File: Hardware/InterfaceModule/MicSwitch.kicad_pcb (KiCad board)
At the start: 2 copper layers, 76 x 76 mm, 21 parts, among them J10 External MIC IN, J6 D-700 MIC, J7 TS-480 MIC, J8 D-700 EXT.SP 1, J9 TS-480 EXT.SP, K1 FINDER-40.52, K2 FINDER-40.52, K3 FINDER-40.52, K4 FINDER-40.52, K5 FINDER-40.52, K6 FINDER-40.52, K7 FINDER-40.52, K8 FINDER-40.52

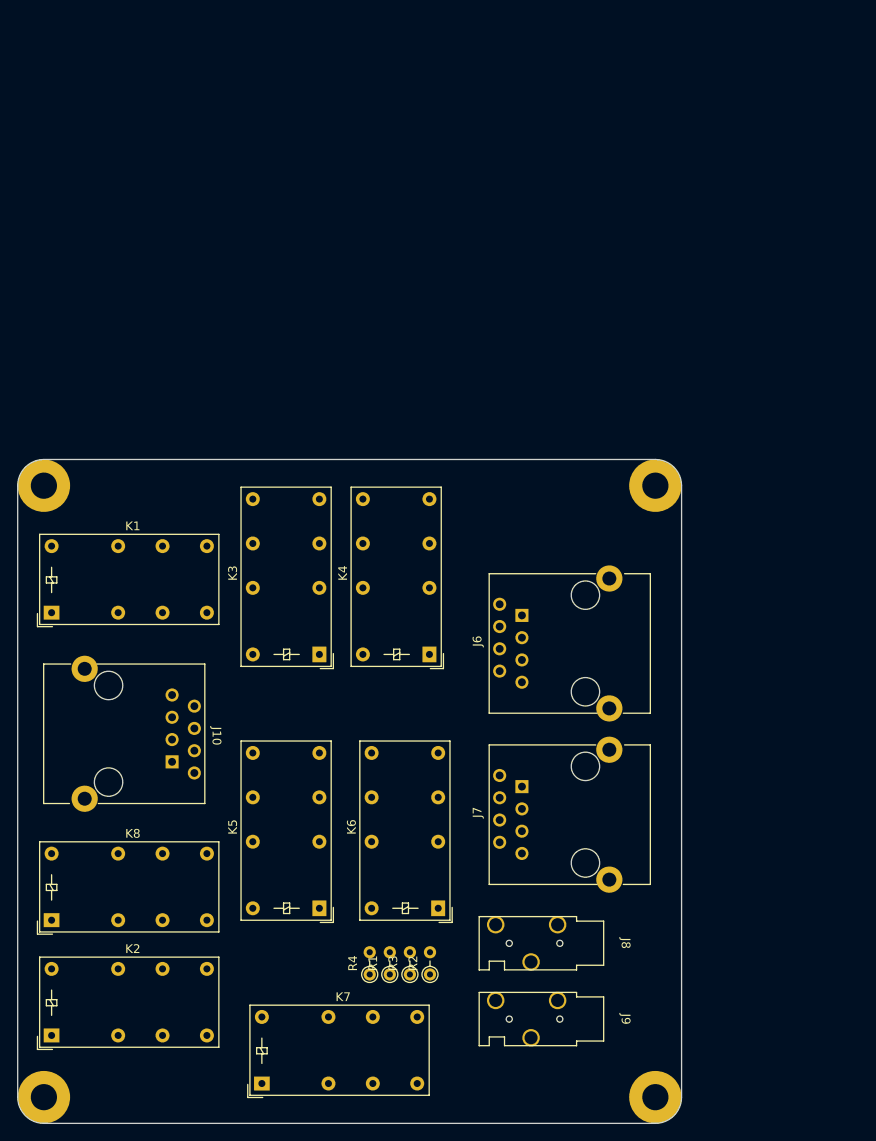
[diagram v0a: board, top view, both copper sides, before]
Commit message: Updated silkscreen dates, corrected gerber files
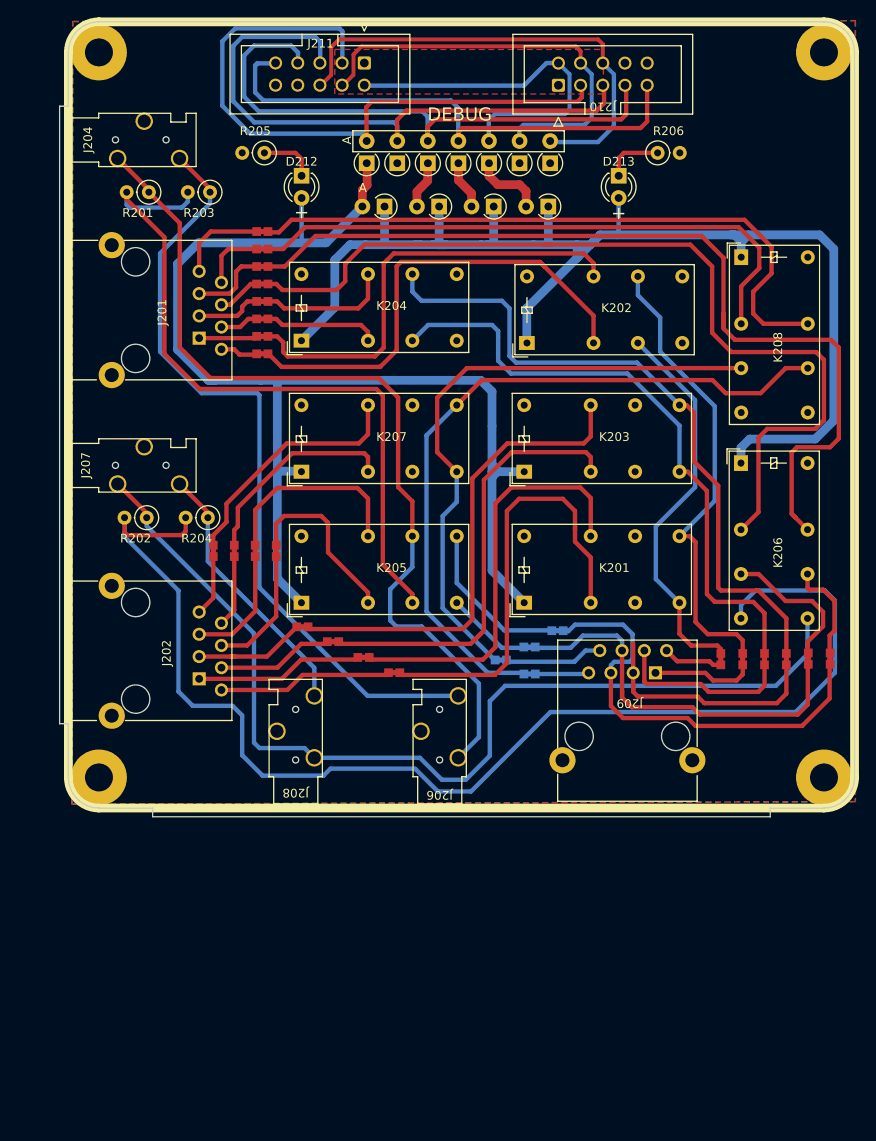
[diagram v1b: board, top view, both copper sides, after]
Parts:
- removed H1, H2, H3, H4: MountingHole_Pad, 
- removed J10: External MIC IN, libraries:Mystery_RJ45
- removed J6: D-700 MIC, libraries:Mystery_RJ45
- removed J7: TS-480 MIC, libraries:Mystery_RJ45
- removed J8: D-700 EXT.SP 1, libraries:Mystery_3.5mm
- removed J9: TS-480 EXT.SP, libraries:Mystery_3.5mm
- removed K1, K2, K3, K4, K5, K6, K7, K8: FINDER-40.52, Relay_THT:Relay_DPDT_Finder_30.22
- removed R1, R2: 3.9Ohm, Resistor_THT:R_Axial_DIN0204_L3.6mm_D1.6mm_P2.54mm_Vertical
- removed R3, R4: 470Ohm, Resistor_THT:R_Axial_DIN0204_L3.6mm_D1.6mm_P2.54mm_Vertical
- added D201: D_Small_Filled, Diode_THT:D_A-405_P2.54mm_Vertical_AnodeUp, F.Cu at (141.7, 26.7)
- added D202: D_Small_Filled, Diode_THT:D_A-405_P2.54mm_Vertical_AnodeUp, F.Cu at (145.2, 26.7)
- added D203: D_Small_Filled, Diode_THT:D_A-405_P2.54mm_Vertical_AnodeUp, F.Cu at (148.7, 26.7)
- added D204: D_Small_Filled, Diode_THT:D_A-405_P2.54mm_Vertical_AnodeUp, F.Cu at (152.2, 26.7)
- added D205: D_Small_Filled, Diode_THT:D_A-405_P2.54mm_Vertical_AnodeUp, F.Cu at (155.7, 26.7)
- added D206: D_Small_Filled, Diode_THT:D_A-405_P2.54mm_Vertical_AnodeUp, F.Cu at (159.2, 26.7)
- added D207: D_Small_Filled, Diode_THT:D_A-405_P2.54mm_Vertical_AnodeUp, F.Cu at (162.7, 26.7)
- added D208: D_Small_Filled, Diode_THT:D_A-405_P2.54mm_Vertical_AnodeUp, F.Cu at (143.7, 31.6)
- added D209: D_Small_Filled, Diode_THT:D_A-405_P2.54mm_Vertical_AnodeUp, F.Cu at (149.9, 31.6)
- added D210: D_Small_Filled, Diode_THT:D_A-405_P2.54mm_Vertical_AnodeUp, F.Cu at (156.2, 31.6)
- added D211: D_Small_Filled, Diode_THT:D_A-405_P2.54mm_Vertical_AnodeUp, F.Cu at (162.4, 31.6)
- added D212: LED, LED_THT:LED_D3.0mm, F.Cu at (134.2, 28.1)
- added D213: LED, LED_THT:LED_D3.0mm, F.Cu at (170.5, 28.1)
- added G***: LOGO, libraries:LogoLargeInvert, B.Cu at (163.6, 57.9)
- added H201: Mounting Hole, libraries:M3_Mounting, F.Cu at (111.0, 97.0)
- added H202: Mounting Hole, libraries:M3_Mounting, F.Cu at (194.0, 14.0)
- added H203: Mounting Hole, libraries:M3_Mounting, F.Cu at (111.0, 14.0)
- added H204: Mounting Hole, libraries:M3_Mounting, F.Cu at (194.0, 97.0)
- added J201: D-700 MIC, libraries:Mystery_RJ45, F.Cu at (122.5, 46.7)
- added J202: TS-480 MIC, libraries:Mystery_RJ45, F.Cu at (122.5, 85.7)
- added J204: D-700 EXT.SP 1, libraries:Mystery_3.5mm, F.Cu at (112.9, 24.0)
- added J206: D-700 EXT.SP Passthrough, libraries:Mystery_3.5mm, F.Cu at (150.0, 95.0)
- added J207: TS-480 EXT.SP, libraries:Mystery_3.5mm, F.Cu at (112.9, 61.3)
- added J208: TS-480 EXT.SP Passthrough, libraries:Mystery_3.5mm, F.Cu at (133.5, 95.0)
- added J209: External MIC IN, libraries:Mystery_RJ45, F.Cu at (174.7, 85.0)
- added J210: 2x05 IDC Header - IN, Connector_IDC:IDC-Header_2x05_P2.54mm_Vertical, F.Cu at (163.6, 17.8)
- added J211: 2x05 IDC Header - OUT, Connector_IDC:IDC-Header_2x05_P2.54mm_Vertical, F.Cu at (141.4, 15.2)
- added JP201: Jumper_2_Bridged, libraries:1.0mm_Bridge, F.Cu at (129.7, 46.5)
- added JP202: Jumper_2_Bridged, libraries:1.0mm_Bridge, F.Cu at (129.7, 48.5)
- added JP203: Jumper_2_Bridged, libraries:1.0mm_Bridge, F.Cu at (129.7, 42.5)
- added JP204: Jumper_2_Bridged, libraries:1.0mm_Bridge, F.Cu at (129.7, 44.5)
- added JP205: Jumper_2_Bridged, libraries:1.0mm_Bridge, F.Cu at (129.7, 38.5)
- added JP206: Jumper_2_Bridged, libraries:1.0mm_Bridge, F.Cu at (129.7, 40.5)
- added JP207: Jumper_2_Bridged, libraries:1.0mm_Bridge, F.Cu at (129.7, 34.5)
- added JP208: Jumper_2_Bridged, libraries:1.0mm_Bridge, F.Cu at (141.3, 83.3)
- added JP209: Jumper_2_Bridged, libraries:1.0mm_Bridge, F.Cu at (129.7, 36.5)
- added JP210: Jumper_2_Bridged, libraries:1.0mm_Bridge, F.Cu at (144.8, 85.0)
- added JP211: Jumper_2_Bridged, libraries:1.0mm_Bridge, F.Cu at (134.3, 79.8)
- added JP212: Jumper_2_Bridged, libraries:1.0mm_Bridge, F.Cu at (137.8, 81.5)
- added JP213: Jumper_2_Bridged, libraries:1.0mm_Bridge, F.Cu at (128.9, 71.1)
- added JP214: Jumper_2_Bridged, libraries:1.0mm_Bridge, F.Cu at (131.3, 71.1)
- added JP215: Jumper_2_Bridged, libraries:1.0mm_Bridge, F.Cu at (124.1, 71.1)
- added JP216: Jumper_2_Bridged, libraries:1.0mm_Bridge, F.Cu at (126.5, 71.1)
- added JP217: Jumper_2_Bridged, libraries:1.0mm_Bridge, F.Cu at (184.7, 83.5)
- added JP218: Jumper_2_Bridged, libraries:1.0mm_Bridge, F.Cu at (182.2, 83.5)
- added JP219: Jumper_2_Bridged, libraries:1.0mm_Bridge, F.Cu at (189.7, 83.5)
- added JP220: Jumper_2_Bridged, libraries:1.0mm_Bridge, F.Cu at (187.2, 83.5)
- added JP223: Jumper_2_Bridged, libraries:1.0mm_Bridge, B.Cu at (160.3, 85.2)
- added JP224: Jumper_2_Bridged, libraries:1.0mm_Bridge, B.Cu at (157.0, 83.6)
- added JP225: Jumper_2_Bridged, libraries:1.0mm_Bridge, F.Cu at (194.7, 83.4)
- added JP225: Jumper_2_Bridged, libraries:1.0mm_Bridge, F.Cu at (192.2, 83.4)
- added JP225: Jumper_2_Bridged, libraries:1.0mm_Bridge, B.Cu at (163.5, 80.2)
- added JP225: Jumper_2_Bridged, libraries:1.0mm_Bridge, B.Cu at (160.3, 82.1)
- added K201: FINDER-40.52, Relay_THT:Relay_DPDT_Finder_30.22, F.Cu at (159.7, 77.0)
- added K202: FINDER-40.52, Relay_THT:Relay_DPDT_Finder_30.22, F.Cu at (160.0, 47.3)
- added K203: FINDER-40.52, Relay_THT:Relay_DPDT_Finder_30.22, F.Cu at (159.7, 62.0)
- added K204: FINDER-40.52, Relay_THT:Relay_DPDT_Finder_30.22, F.Cu at (134.2, 47.0)
- added K205: FINDER-40.52, Relay_THT:Relay_DPDT_Finder_30.22, F.Cu at (134.2, 77.0)
- added K206: FINDER-40.52, Relay_THT:Relay_DPDT_Finder_30.22, F.Cu at (184.5, 61.0)
- added K207: FINDER-40.52, Relay_THT:Relay_DPDT_Finder_30.22, F.Cu at (134.2, 62.0)
- added K208: FINDER-40.52, Relay_THT:Relay_DPDT_Finder_30.22, F.Cu at (184.5, 37.4)
- added R201: 3.9Ohm, Resistor_THT:R_Axial_DIN0207_L6.3mm_D2.5mm_P2.54mm_Vertical, F.Cu at (116.7, 30.0)
- added R202: 3.9Ohm, Resistor_THT:R_Axial_DIN0207_L6.3mm_D2.5mm_P2.54mm_Vertical, F.Cu at (116.5, 67.3)
- added R203: 470Ohm, Resistor_THT:R_Axial_DIN0207_L6.3mm_D2.5mm_P2.54mm_Vertical, F.Cu at (123.7, 30.0)
- added R204: 470Ohm, Resistor_THT:R_Axial_DIN0207_L6.3mm_D2.5mm_P2.54mm_Vertical, F.Cu at (123.5, 67.3)
- added R205: 680Ω, Resistor_THT:R_Axial_DIN0207_L6.3mm_D2.5mm_P2.54mm_Vertical, F.Cu at (129.9, 25.5)
- added R206: 680Ω, Resistor_THT:R_Axial_DIN0207_L6.3mm_D2.5mm_P2.54mm_Vertical, F.Cu at (175.0, 25.5)
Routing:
- net /Microphone Switching/RightBank: track 0.00 -> 147.3 mm
- net /Microphone Switching/Knob_Pos_1: track 0.00 -> 144.5 mm
- net Net-(K206-Pad14): track 0.00 -> 143.6 mm
- net /Microphone Switching/480_SP_S: track 0.00 -> 114.9 mm
- net /Microphone Switching/D700_MIC: track 0.00 -> 105.0 mm
- net /Microphone Switching/D700_MICGND: track 0.00 -> 104.8 mm
- net /Microphone Switching/D700_SP_S: track 0.00 -> 102.2 mm
- net /Microphone Switching/D700_SP_T: track 0.00 -> 89.3 mm
- net /Microphone Switching/EXT_MICGND: track 0.00 -> 83.2 mm
- net /Microphone Switching/EXT_NC: track 0.00 -> 82.4 mm
- net Net-(K205-Pad12): track 0.00 -> 82.3 mm
- net /Microphone Switching/EXT_GND: track 0.00 -> 77.7 mm
- net /Microphone Switching/Knob_Pos_1_Raw: track 0.00 -> 75.2 mm
- net /Microphone Switching/D700_NC: track 0.00 -> 74.8 mm
- net /Microphone Switching/EXT_MIC: track 0.00 -> 74.1 mm
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- added copper zone on F.Cu, net +12P
- added copper zone on B.Cu, net GND
- added copper zone on F.Cu, net GND
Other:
- board size 76 x 76 mm -> 91 x 91 mm
- board text added: "+"
- board text added: "D-700"
- board text added: "D-700 MIC"
- board text added: "DEBUG"
- board text added: "Ext. SP"
- board text added: "External MIC In"
- board text added: "IN"
- board text added: "MIC Module Rev 1. Feb 27th, 2023 Thomas Francois"
- board text added: "OUT"
- board text added: "Pass Thru Ext. SP"
- board text added: "TS-480"
- board text added: "TS-480 MIC"
